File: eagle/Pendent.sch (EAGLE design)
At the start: 38 parts, among them Q1 CMA-4544PF-W, Q2 MPSA42, Q3 8/16/20MHz, U1 MAX9814TDFN14, U2 LF50ABDT-TR, U3 ATMEGA328

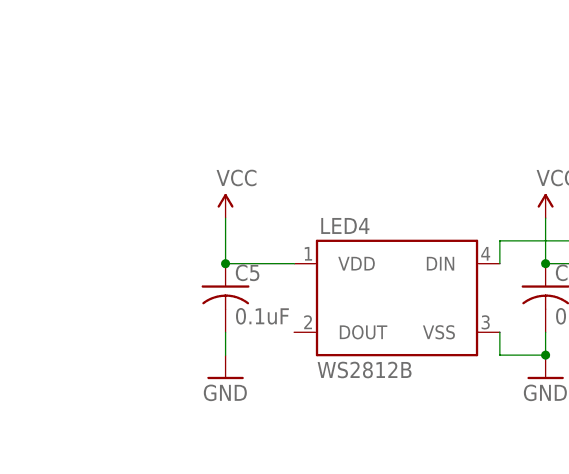
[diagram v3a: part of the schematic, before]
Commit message: Add External LED Connection
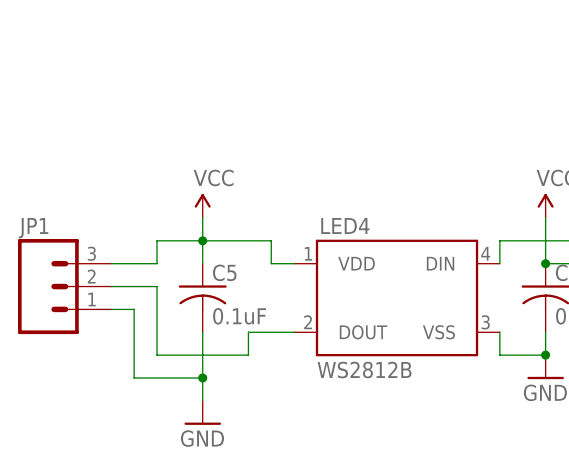
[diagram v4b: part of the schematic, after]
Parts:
- added JP1: (no value), SparkFun-Connectors:M03PTH
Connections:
- new net N$6: JP1.2, LED4.DOUT
- net GND: now also JP1.1
- net VCC: now also JP1.3
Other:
- moved on the sheet: C5
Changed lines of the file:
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@@
 <part name="S3" library="Testing" deviceset="SWITCH-MOMENTARY-2" device="SMD-ALT01" value="RESET"/>
 <part name="Q3" library="Testing" deviceset="RESONATOR" device="1:1" value="8/16/20MHz"/>
+<part name="JP1" library="SparkFun-Connectors" deviceset="M03" device="PTH"/>
 </parts>
 <sheets>
@@
 <instance part="GND4" gate="1" x="15.24" y="104.14"/>
 <instance part="C4" gate="G$1" x="15.24" y="114.3"/>
-<instance part="P+5" gate="1" x="-20.32" y="121.92"/>
-<instance part="GND7" gate="1" x="-20.32" y="104.14"/>
-<instance part="C5" gate="G$1" x="-20.32" y="114.3"/>
+<instance part="P+5" gate="1" x="-22.86" y="121.92"/>
+<instance part="GND7" gate="1" x="-22.86" y="99.06"/>
+<instance part="C5" gate="G$1" x="-22.86" y="114.3"/>
 <instance part="U2" gate="G$1" x="71.12" y="144.78"/>
 <instance part="U$3" gate="G$1" x="38.1" y="142.24" rot="R270"/>
@@
 <attribute name="VALUE" x="92.202" y="233.172" size="1.778" layer="96"/>
 </instance>
+<instance part="JP1" gate="G$1" x="-40.64" y="114.3"/>
 </instances>
 <busses>
@@
 <pinref part="P+5" gate="1" pin="VCC"/>
 <pinref part="C5" gate="G$1" pin="1"/>
-<wire x1="-20.32" y1="121.92" x2="-20.32" y2="116.84" width="0.1524" layer="91"/>
+<wire x1="-22.86" y1="121.92" x2="-22.86" y2="119.38" width="0.1524" layer="91"/>
+<wire x1="-22.86" y1="119.38" x2="-22.86" y2="116.84" width="0.1524" layer="91"/>
+<wire x1="-22.86" y1="119.38" x2="-15.24" y2="119.38" width="0.1524" layer="91"/>
+<junction x="-22.86" y="119.38"/>
+<wire x1="-15.24" y1="119.38" x2="-15.24" y2="116.84" width="0.1524" layer="91"/>
 <pinref part="LED4" gate="G$1" pin="VDD"/>
-<wire x1="-20.32" y1="116.84" x2="-12.7" y2="116.84" width="0.1524" layer="91"/>
-<junction x="-20.32" y="116.84"/>
+<wire x1="-15.24" y1="116.84" x2="-12.7" y2="116.84" width="0.1524" layer="91"/>
+<pinref part="JP1" gate="G$1" pin="3"/>
+<wire x1="-33.02" y1="116.84" x2="-27.94" y2="116.84" width="0.1524" layer="91"/>
+<wire x1="-27.94" y1="116.84" x2="-27.94" y2="119.38" width="0.1524" layer="91"/>
+<wire x1="-27.94" y1="119.38" x2="-22.86" y2="119.38" width="0.1524" layer="91"/>
 </segment>
 <segment>
@@
 <pinref part="C5" gate="G$1" pin="2"/>
 <pinref part="GND7" gate="1" pin="GND"/>
-<wire x1="-20.32" y1="109.22" x2="-20.32" y2="106.68" width="0.1524" layer="91"/>
+<wire x1="-22.86" y1="109.22" x2="-22.86" y2="104.14" width="0.1524" layer="91"/>
+<pinref part="JP1" gate="G$1" pin="1"/>
+<wire x1="-22.86" y1="104.14" x2="-22.86" y2="101.6" width="0.1524" layer="91"/>
+<wire x1="-33.02" y1="111.76" x2="-30.48" y2="111.76" width="0.1524" layer="91"/>
+<wire x1="-30.48" y1="111.76" x2="-30.48" y2="104.14" width="0.1524" layer="91"/>
+<wire x1="-30.48" y1="104.14" x2="-22.86" y2="104.14" width="0.1524" layer="91"/>
+<junction x="-22.86" y="104.14"/>
 </segment>
 <segment>
@@
 </segment>
 </net>
+<net name="N$6" class="0">
+<segment>
+<pinref part="LED4" gate="G$1" pin="DOUT"/>
+<wire x1="-12.7" y1="109.22" x2="-17.78" y2="109.22" width="0.1524" layer="91"/>
+<wire x1="-17.78" y1="109.22" x2="-17.78" y2="106.68" width="0.1524" layer="91"/>
+<wire x1="-17.78" y1="106.68" x2="-27.94" y2="106.68" width="0.1524" layer="91"/>
+<wire x1="-27.94" y1="106.68" x2="-27.94" y2="114.3" width="0.1524" layer="91"/>
+<pinref part="JP1" gate="G$1" pin="2"/>
+<wire x1="-27.94" y1="114.3" x2="-33.02" y2="114.3" width="0.1524" layer="91"/>
+</segment>
+</net>

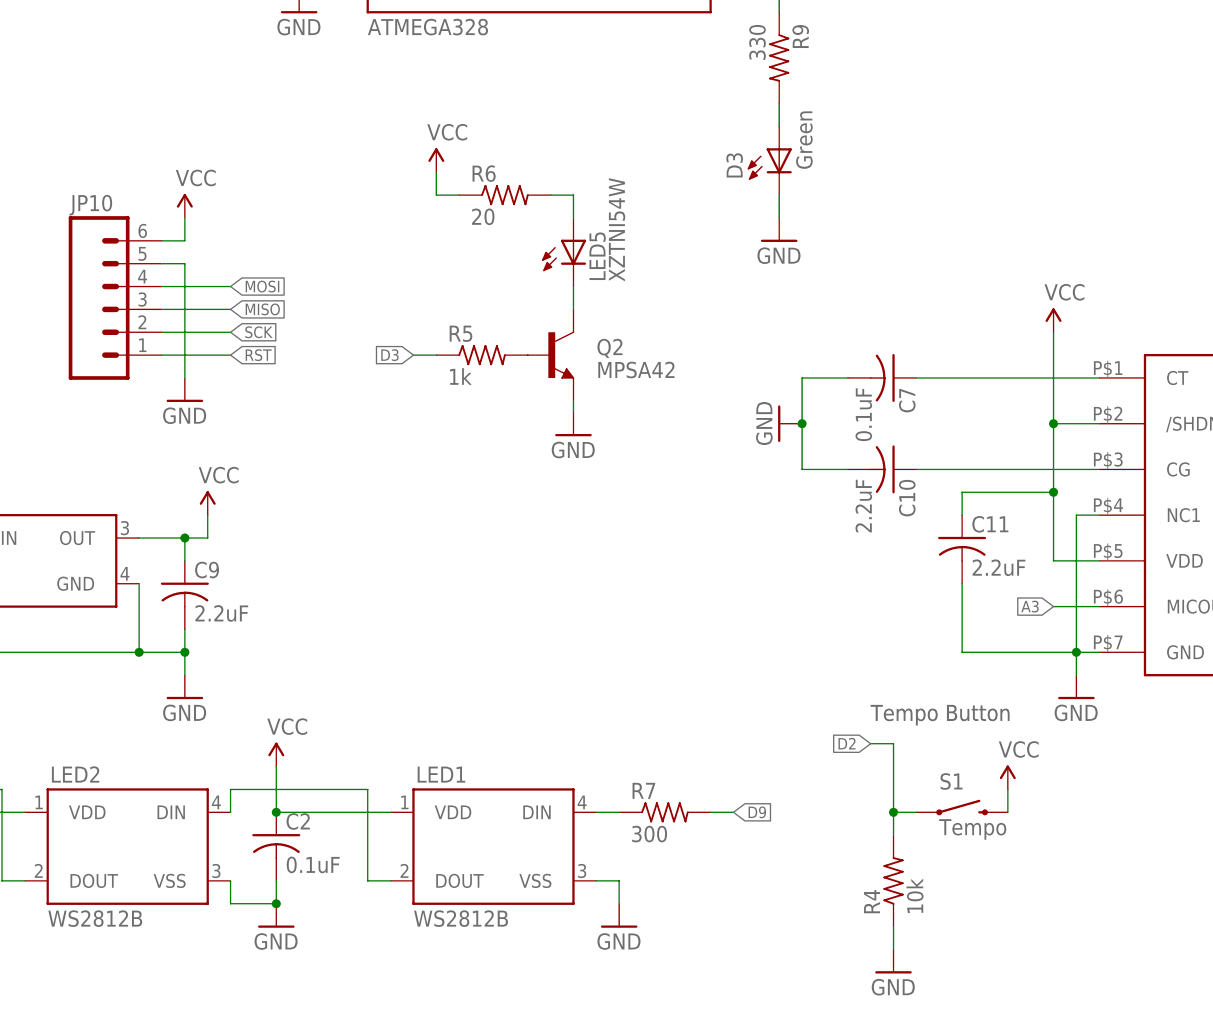
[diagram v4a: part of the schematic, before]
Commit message: Switch to correct battery footprint, switch to V13 isp
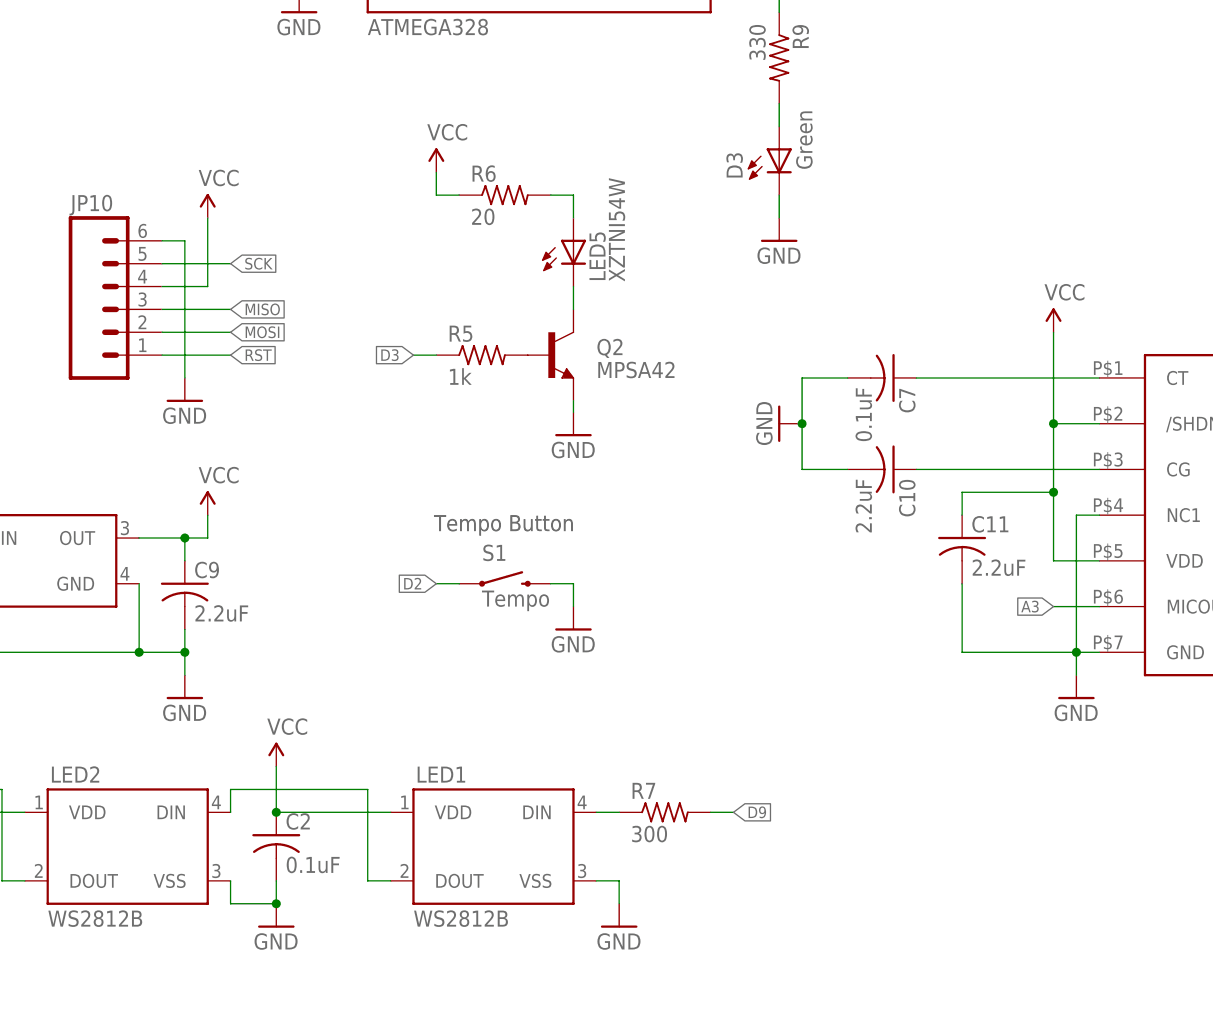
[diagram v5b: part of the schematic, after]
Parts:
- removed R4: 10k, adafruit:R-US_R0805
- LED5: device adafruit:LEDCHIP-LED0805 -> led:LED5MM
- U$3: device SparkFun-Electromechanical:BATTERY20SMD -> bag_eagle_lib:BATTERY20SMD
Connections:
- net D2: no longer R4.2
- net GND: now also JP10.6, S1.2; no longer JP10.5, R4.1
- net MOSI: now also JP10.2; no longer JP10.4
- net SCK: now also JP10.5; no longer JP10.2
- net VCC: now also JP10.4; no longer JP10.6, S1.2
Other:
- moved on the sheet: S1
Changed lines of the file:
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@@
 <part name="C5" library="adafruit" deviceset="C-US" device="C0805K" value="0.1uF"/>
 <part name="U2" library="BAG" deviceset="LF50ABDT-TR" device=""/>
-<part name="U$3" library="SparkFun-Electromechanical" deviceset="BATTERY" device="20SMD" value="6V"/>
+<part name="U$3" library="bag_eagle_lib" deviceset="BATTERY" device="20SMD" value="6V"/>
 <part name="C8" library="adafruit" deviceset="C-US" device="C0805K" value="2.2uF"/>
 <part name="C9" library="adafruit" deviceset="C-US" device="C0805K" value="2.2uF"/>
@@
 <part name="GND10" library="supply1" deviceset="GND" device=""/>
 <part name="S1" library="SparkFun-Electromechanical" deviceset="SWITCH-MOMENTARY-2" device="SMD-REDUNDANT" value="Tempo"/>
-<part name="P+7" library="SparkFun" deviceset="VCC" device=""/>
 <part name="GND11" library="SparkFun" deviceset="GND" device=""/>
-<part name="R4" library="adafruit" deviceset="R-US_" device="R0805" value="10k"/>
 <part name="Q2" library="SparkFun-DiscreteSemi" deviceset="TRANSISTOR_NPN" device="MPSA42" value="MPSA42"/>
 <part name="GND12" library="supply1" deviceset="GND" device=""/>
 <part name="R5" library="adafruit" deviceset="R-US_" device="R0805" value="1k"/>
-<part name="LED5" library="adafruit" deviceset="LED" device="CHIP-LED0805" value="XZTNI54W"/>
+<part name="LED5" library="led" deviceset="LED" device="5MM" value="XZTNI54W"/>
 <part name="R6" library="adafruit" deviceset="R-US_" device="R0805" value="20"/>
 <part name="P+8" library="SparkFun" deviceset="VCC" device=""/>
@@
 <sheet>
 <plain>
-<text x="162.56" y="127" size="1.778" layer="97">Tempo Button</text>
+<text x="114.046" y="148.082" size="1.778" layer="97">Tempo Button</text>
 </plain>
 <instances>
@@
 <instance part="P+1" gate="1" x="182.88" y="170.18"/>
 <instance part="GND10" gate="1" x="185.42" y="129.54"/>
-<instance part="S1" gate="G$1" x="172.72" y="116.84"/>
-<instance part="P+7" gate="1" x="177.8" y="119.38"/>
-<instance part="GND11" gate="1" x="165.1" y="99.06"/>
-<instance part="R4" gate="G$1" x="165.1" y="109.22" rot="R90"/>
+<instance part="S1" gate="G$1" x="121.92" y="142.24"/>
+<instance part="GND11" gate="1" x="129.54" y="137.16"/>
 <instance part="Q2" gate="G$1" x="127" y="167.64"/>
 <instance part="GND12" gate="1" x="129.54" y="158.75"/>
@@
 <instance part="JP10" gate="G$1" x="78.74" y="172.72"/>
 <instance part="GND15" gate="1" x="86.36" y="162.56"/>
-<instance part="SUPPLY9" gate="1" x="86.36" y="182.88"/>
+<instance part="SUPPLY9" gate="1" x="88.9" y="182.88"/>
 <instance part="R8" gate="G$1" x="76.2" y="274.32" rot="R90"/>
 <instance part="GND16" gate="1" x="76.2" y="248.92"/>
@@
 </segment>
 <segment>
-<pinref part="S1" gate="G$1" pin="2"/>
-<pinref part="P+7" gate="1" pin="VCC"/>
-<wire x1="177.8" y1="116.84" x2="177.8" y2="119.38" width="0.1524" layer="91"/>
-</segment>
-<segment>
 <pinref part="P+8" gate="1" pin="VCC"/>
 <wire x1="114.3" y1="187.96" x2="114.3" y2="185.42" width="0.1524" layer="91"/>
 <pinref part="R6" gate="G$1" pin="1"/>
 <wire x1="114.3" y1="185.42" x2="116.84" y2="185.42" width="0.1524" layer="91"/>
-</segment>
-<segment>
-<pinref part="JP10" gate="G$1" pin="6"/>
-<wire x1="83.82" y1="180.34" x2="86.36" y2="180.34" width="0.1524" layer="91"/>
-<wire x1="86.36" y1="180.34" x2="86.36" y2="182.88" width="0.1524" layer="91"/>
-<pinref part="SUPPLY9" gate="1" pin="VCC"/>
 </segment>
 <segment>
@@
 <pinref part="U3" gate="G$1" pin="VCC@2"/>
 <pinref part="P+10" gate="G$1" pin="3.3V"/>
+</segment>
+<segment>
+<pinref part="SUPPLY9" gate="1" pin="VCC"/>
+<wire x1="88.9" y1="182.88" x2="88.9" y2="175.26" width="0.1524" layer="91"/>
+<pinref part="JP10" gate="G$1" pin="4"/>
+<wire x1="83.82" y1="175.26" x2="88.9" y2="175.26" width="0.1524" layer="91"/>
 </segment>
 </net>
@@
 </segment>
 <segment>
-<pinref part="R4" gate="G$1" pin="1"/>
 <pinref part="GND11" gate="1" pin="GND"/>
-<wire x1="165.1" y1="104.14" x2="165.1" y2="101.6" width="0.1524" layer="91"/>
+<wire x1="129.54" y1="142.24" x2="129.54" y2="139.7" width="0.1524" layer="91"/>
+<pinref part="S1" gate="G$1" pin="2"/>
+<wire x1="127" y1="142.24" x2="129.54" y2="142.24" width="0.1524" layer="91"/>
 </segment>
 <segment>
@@
 </segment>
 <segment>
-<pinref part="JP10" gate="G$1" pin="5"/>
-<wire x1="83.82" y1="177.8" x2="86.36" y2="177.8" width="0.1524" layer="91"/>
-<wire x1="86.36" y1="177.8" x2="86.36" y2="165.1" width="0.1524" layer="91"/>
+<wire x1="86.36" y1="180.34" x2="86.36" y2="165.1" width="0.1524" layer="91"/>
 <pinref part="GND15" gate="1" pin="GND"/>
+<pinref part="JP10" gate="G$1" pin="6"/>
+<wire x1="83.82" y1="180.34" x2="86.36" y2="180.34" width="0.1524" layer="91"/>
 </segment>
 <segment>
@@
 <net name="MOSI" class="0">
 <segment>
-<label x="91.44" y="175.26" size="1.27" layer="95" xref="yes"/>
-<pinref part="JP10" gate="G$1" pin="4"/>
-<wire x1="83.82" y1="175.26" x2="91.44" y2="175.26" width="0.1524" layer="91"/>
-</segment>
-<segment>
 <wire x1="149.86" y1="213.36" x2="152.4" y2="213.36" width="0.1524" layer="91"/>
 <pinref part="U3" gate="G$1" pin="PB3(MOSI/OC2)"/>
 <label x="152.4" y="213.36" size="1.27" layer="95" xref="yes"/>
 </segment>
+<segment>
+<pinref part="JP10" gate="G$1" pin="2"/>
+<wire x1="83.82" y1="170.18" x2="91.44" y2="170.18" width="0.1524" layer="91"/>
+<label x="91.44" y="170.18" size="1.27" layer="95" xref="yes"/>
+</segment>
 </net>
 <net name="MISO" class="0">
-<segment>
-<label x="91.44" y="172.72" size="1.27" layer="95" xref="yes"/>
-<pinref part="JP10" gate="G$1" pin="3"/>
-<wire x1="83.82" y1="172.72" x2="91.44" y2="172.72" width="0.1524" layer="91"/>
-</segment>
 <segment>
 <wire x1="149.86" y1="210.82" x2="152.4" y2="210.82" width="0.1524" layer="91"/>
@@
 <label x="152.4" y="210.82" size="1.27" layer="95" xref="yes"/>
 </segment>
+<segment>
+<pinref part="JP10" gate="G$1" pin="3"/>
+<wire x1="83.82" y1="172.72" x2="91.44" y2="172.72" width="0.1524" layer="91"/>
+<label x="91.44" y="172.72" size="1.27" layer="95" xref="yes"/>
+</segment>
 </net>
 <net name="SCK" class="0">
-<segment>
-<label x="91.44" y="170.18" size="1.27" layer="95" xref="yes"/>
-<pinref part="JP10" gate="G$1" pin="2"/>
-<wire x1="83.82" y1="170.18" x2="91.44" y2="170.18" width="0.1524" layer="91"/>
-</segment>
 <segment>
 <wire x1="152.4" y1="208.28" x2="152.4" y2="205.74" width="0.1524" layer="91"/>
@@
 <wire x1="152.4" y1="208.28" x2="154.94" y2="208.28" width="0.1524" layer="91"/>
 <label x="154.94" y="208.28" size="1.27" layer="95" xref="yes"/>
+</segment>
+<segment>
+<pinref part="JP10" gate="G$1" pin="5"/>
+<wire x1="83.82" y1="177.8" x2="91.44" y2="177.8" width="0.1524" layer="91"/>
+<label x="91.44" y="177.8" size="1.27" layer="95" xref="yes"/>
 </segment>
 </net>
@@
 </segment>
 <segment>
-<pinref part="R4" gate="G$1" pin="2"/>
-<wire x1="165.1" y1="114.3" x2="165.1" y2="116.84" width="0.1524" layer="91"/>
+<wire x1="116.84" y1="142.24" x2="114.3" y2="142.24" width="0.1524" layer="91"/>
+<label x="114.3" y="142.24" size="1.27" layer="95" rot="R180" xref="yes"/>
 <pinref part="S1" gate="G$1" pin="1"/>
-<wire x1="165.1" y1="116.84" x2="167.64" y2="116.84" width="0.1524" layer="91"/>
-<wire x1="165.1" y1="116.84" x2="165.1" y2="124.46" width="0.1524" layer="91"/>
-<junction x="165.1" y="116.84"/>
-<wire x1="165.1" y1="124.46" x2="162.56" y2="124.46" width="0.1524" layer="91"/>
-<label x="162.56" y="124.46" size="1.27" layer="95" rot="R180" xref="yes"/>
-</segment>
-</net>
+</segment>
+</net>

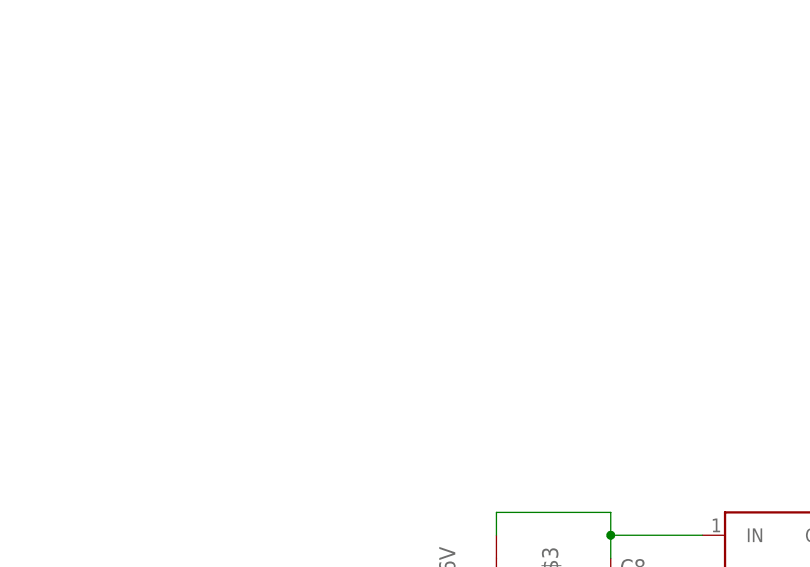
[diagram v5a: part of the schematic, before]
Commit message: Add IR Receiver
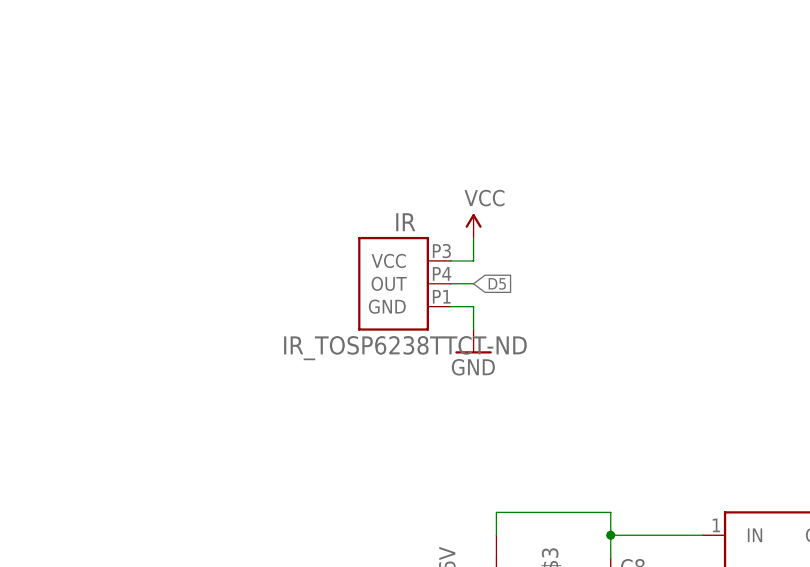
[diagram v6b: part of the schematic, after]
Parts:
- added IR: IR_TOSP6238TTCT-ND, bg_eagle_lib:IR_TOSP6238TTCT-ND
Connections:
- net D5: now also IR.OUT
- net GND: now also IR.GND
- net VCC: now also IR.VCC
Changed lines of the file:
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@@
 </variantdefs>
 <classes>
-<class number="0" name="default" width="0.2032" drill="0">
+<class number="0" name="default" width="0.254" drill="0.381">
+<clearance class="0" value="0.254"/>
 </class>
-<class number="1" name="vcc" width="0.254" drill="0">
+<class number="1" name="vcc" width="0.508" drill="0.381">
+<clearance class="1" value="0.254"/>
 </class>
 </classes>
@@
 <part name="Q3" library="Testing" deviceset="RESONATOR" device="1:1" value="8/16/20MHz"/>
 <part name="JP1" library="SparkFun-Connectors" deviceset="M03" device="PTH"/>
+<part name="IR" library="bg_eagle_lib" deviceset="IR_TOSP62" device="38TTCT-ND" value="IR_TOSP6238TTCT-ND"/>
+<part name="SUPPLY1" library="SparkFun-Aesthetics" deviceset="VCC" device=""/>
+<part name="GND17" library="SparkFun-Aesthetics" deviceset="GND" device=""/>
 </parts>
 <sheets>
@@
 </instance>
 <instance part="JP1" gate="G$1" x="-40.64" y="114.3"/>
+<instance part="IR" gate="TOSP62" x="27.94" y="175.26"/>
+<instance part="SUPPLY1" gate="1" x="35.56" y="180.34"/>
+<instance part="GND17" gate="1" x="35.56" y="167.64"/>
 </instances>
 <busses>
@@
 <pinref part="JP10" gate="G$1" pin="4"/>
 <wire x1="83.82" y1="175.26" x2="88.9" y2="175.26" width="0.1524" layer="91"/>
+</segment>
+<segment>
+<pinref part="IR" gate="TOSP62" pin="VCC"/>
+<pinref part="SUPPLY1" gate="1" pin="VCC"/>
+<wire x1="33.02" y1="177.8" x2="35.56" y2="177.8" width="0.1524" layer="91"/>
+<wire x1="35.56" y1="177.8" x2="35.56" y2="180.34" width="0.1524" layer="91"/>
 </segment>
 </net>
@@
 <pinref part="GND21" gate="1" pin="GND"/>
 </segment>
+<segment>
+<pinref part="IR" gate="TOSP62" pin="GND"/>
+<pinref part="GND17" gate="1" pin="GND"/>
+<wire x1="33.02" y1="172.72" x2="35.56" y2="172.72" width="0.1524" layer="91"/>
+<wire x1="35.56" y1="172.72" x2="35.56" y2="170.18" width="0.1524" layer="91"/>
+</segment>
 </net>
 <net name="N$2" class="0">
@@
 <label x="152.4" y="231.14" size="1.27" layer="95" xref="yes"/>
 </segment>
-</net>
+<segment>
+<pinref part="IR" gate="TOSP62" pin="OUT"/>
+<wire x1="33.02" y1="175.26" x2="35.56" y2="175.26" width="0.1524" layer="91"/>
+<label x="35.56" y="175.26" size="1.27" layer="95" xref="yes"/>
+</segment>
+</net>
